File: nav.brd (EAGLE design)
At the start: 160 x 100 mm, 61 parts, among them IC1 FT230XQ, SW1 DHT-4235A, U2 ATMEGA2560-16AU100A-M, U3 MPL3115A2, Y1 16MHz

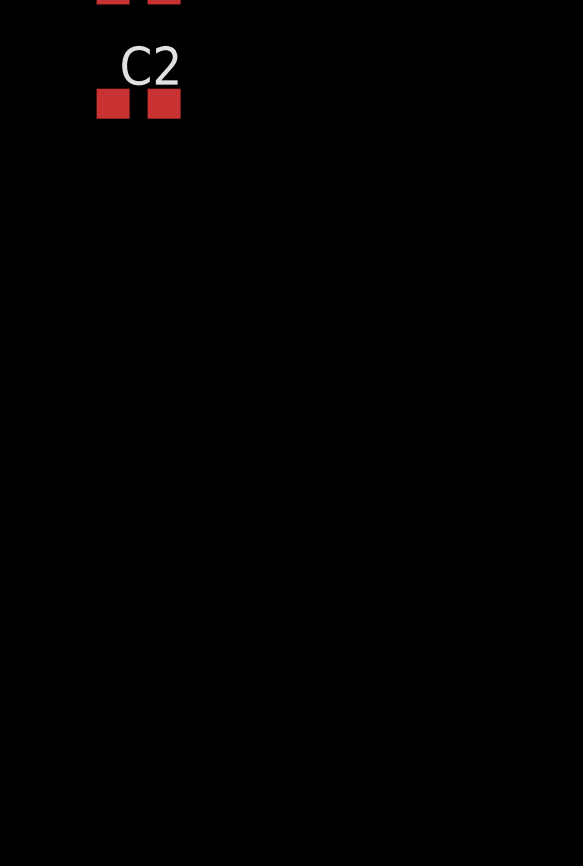
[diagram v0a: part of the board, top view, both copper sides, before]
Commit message: Added Barometer
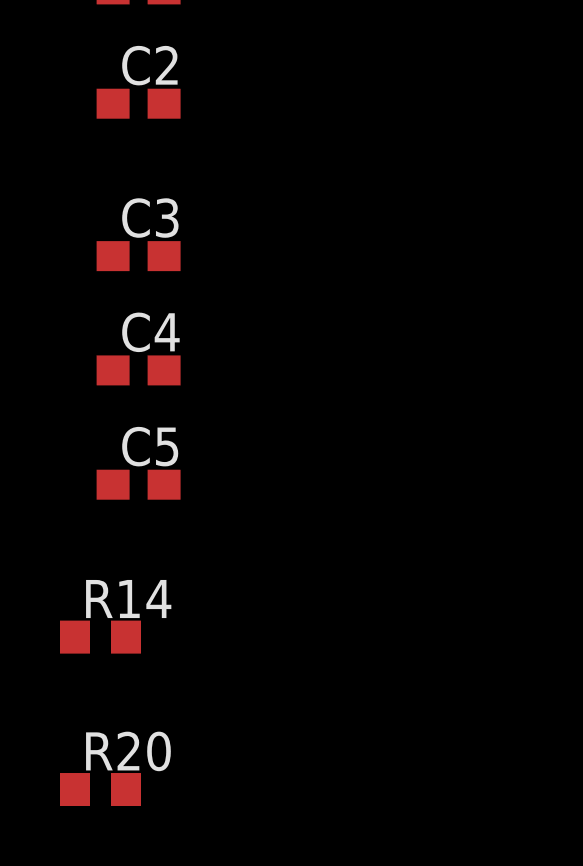
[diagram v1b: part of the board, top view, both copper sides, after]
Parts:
- added C3: 10u, resistor:C0603
- added C4, C5: 100n, resistor:C0603
- added R14, R20: (no value), resistor:R0603
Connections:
- removed net CAP: U3.2
- removed net VDD: U3.1
- removed net VDDIO: U3.4
- new net BARO_INT1: U2.89, U3.6
- new net BARO_INT2: U2.88, U3.5
- new net N$17: C5.1, U3.2
- new net SCL: R14.1, U2.43, U3.8
- new net SDA: R20.1, U2.44, U3.7
- net +3V3: now also C3.1, C4.1, R14.2, R20.2, U3.1, U3.4
- net GND: now also C3.2, C4.2, C5.2
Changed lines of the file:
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@@
 <element name="C1" library="resistor" library_urn="urn:adsk.eagle:library:348" package="C0603" package3d_urn="urn:adsk.eagle:package:23616/2" value="1u" x="-3.81" y="-231.14"/>
 <element name="C2" library="resistor" library_urn="urn:adsk.eagle:library:348" package="C0603" package3d_urn="urn:adsk.eagle:package:23616/2" value="0.01u" x="-3.81" y="-234.95"/>
+<element name="C3" library="resistor" library_urn="urn:adsk.eagle:library:348" package="C0603" package3d_urn="urn:adsk.eagle:package:23616/2" value="10u" x="-3.81" y="-240.03"/>
+<element name="C4" library="resistor" library_urn="urn:adsk.eagle:library:348" package="C0603" package3d_urn="urn:adsk.eagle:package:23616/2" value="100n" x="-3.81" y="-243.84"/>
+<element name="C5" library="resistor" library_urn="urn:adsk.eagle:library:348" package="C0603" package3d_urn="urn:adsk.eagle:package:23616/2" value="100n" x="-3.81" y="-247.65"/>
+<element name="R14" library="resistor" library_urn="urn:adsk.eagle:library:348" package="R0603" package3d_urn="urn:adsk.eagle:package:23555/2" value="" x="-5.08" y="-252.73"/>
+<element name="R20" library="resistor" library_urn="urn:adsk.eagle:library:348" package="R0603" package3d_urn="urn:adsk.eagle:package:23555/2" value="" x="-5.08" y="-257.81"/>
 </elements>
 <signals>
@@
 <contactref element="SW1" pad="4"/>
 <contactref element="SW1" pad="3"/>
-<contactref element="U3" pad="3"/>
 <contactref element="U1" pad="P$3"/>
 <contactref element="U1" pad="P$8"/>
@@
 <contactref element="GPS_ANT" pad="GND@4"/>
 <contactref element="GPS_ANT" pad="GND@3"/>
+<contactref element="U3" pad="3"/>
+<contactref element="C5" pad="2"/>
+<contactref element="C3" pad="2"/>
+<contactref element="C4" pad="2"/>
+<wire x1="-2.96" y1="-243.84" x2="-2.96" y2="-247.65" width="0" layer="19" extent="1-1"/>
+<wire x1="-2.96" y1="-240.03" x2="-2.96" y2="-243.84" width="0" layer="19" extent="1-1"/>
+<wire x1="-2.96" y1="-234.95" x2="-2.96" y2="-240.03" width="0" layer="19" extent="1-1"/>
 <wire x1="-2.96" y1="-231.14" x2="-2.96" y2="-234.95" width="0" layer="19" extent="1-1"/>
 <wire x1="4.572" y1="-212.09" x2="-2.96" y2="-231.14" width="0" layer="19" extent="1-1"/>
@@
 <contactref element="C1" pad="1"/>
 <contactref element="C2" pad="1"/>
+<contactref element="U3" pad="1"/>
+<contactref element="U3" pad="4"/>
+<contactref element="C4" pad="1"/>
+<contactref element="C3" pad="1"/>
+<contactref element="R20" pad="2"/>
+<contactref element="R14" pad="2"/>
+<wire x1="-4.66" y1="-240.03" x2="-4.66" y2="-243.84" width="0" layer="19" extent="1-1"/>
+<wire x1="-4.66" y1="-234.95" x2="-4.66" y2="-240.03" width="0" layer="19" extent="1-1"/>
 <wire x1="-4.66" y1="-231.14" x2="-4.66" y2="-234.95" width="0" layer="19" extent="1-1"/>
 <wire x1="-3.81" y1="-228.08" x2="-4.66" y2="-231.14" width="0" layer="19" extent="1-1"/>
+<wire x1="-4.23" y1="-252.73" x2="-4.66" y2="-243.84" width="0" layer="19" extent="1-1"/>
+<wire x1="-4.23" y1="-257.81" x2="-4.23" y2="-252.73" width="0" layer="19" extent="1-1"/>
 <wire x1="-4.23" y1="-199.39" x2="-3.81" y2="-228.08" width="0" layer="19" extent="1-1"/>
-<wire x1="3.93" y1="-181.21" x2="-4.23" y2="-199.39" width="0" layer="19" extent="1-1"/>
+<wire x1="-5.01" y1="-193.645" x2="-4.23" y2="-199.39" width="0" layer="19" extent="1-1"/>
+<wire x1="-5.01" y1="-189.895" x2="-5.01" y2="-193.645" width="0" layer="19" extent="1-1"/>
+<wire x1="3.93" y1="-181.21" x2="-5.01" y2="-189.895" width="0" layer="19" extent="1-1"/>
 <wire x1="36.41" y1="-168.91" x2="3.93" y2="-181.21" width="0" layer="19" extent="1-1"/>
 <wire x1="2.96" y1="-77.47" x2="36.41" y2="-168.91" width="0" layer="19" extent="1-1"/>
@@
 <wire x1="21.59" y1="-172.2" x2="1.69" y2="-175.26" width="0" layer="19" extent="1-1"/>
 </signal>
-<signal name="VDD">
-<contactref element="U3" pad="1"/>
-</signal>
-<signal name="CAP">
-<contactref element="U3" pad="2"/>
-</signal>
-<signal name="VDDIO">
-<contactref element="U3" pad="4"/>
-</signal>
 <signal name="!GPS_RST">
 <contactref element="U1" pad="P$2"/>
@@
 <wire x1="-4.23" y1="-220.98" x2="-3.81" y2="-226.58" width="0" layer="19" extent="1-1"/>
 </signal>
+<signal name="N$17">
+<contactref element="U3" pad="2"/>
+<contactref element="C5" pad="1"/>
+<wire x1="-5.01" y1="-191.145" x2="-4.66" y2="-247.65" width="0" layer="19" extent="1-1"/>
+</signal>
+<signal name="SCL">
+<contactref element="U3" pad="8"/>
+<contactref element="U2" pad="43"/>
+<contactref element="R14" pad="1"/>
+<wire x1="-5.93" y1="-252.73" x2="-2.61" y2="-189.895" width="0" layer="19" extent="1-1"/>
+<wire x1="13.93" y1="-17.9578" x2="-2.61" y2="-189.895" width="0" layer="19" extent="1-1"/>
+</signal>
+<signal name="SDA">
+<contactref element="U3" pad="7"/>
+<contactref element="U2" pad="44"/>
+<contactref element="R20" pad="1"/>
+<wire x1="-5.93" y1="-257.81" x2="-2.61" y2="-191.145" width="0" layer="19" extent="1-1"/>
+<wire x1="14.43" y1="-17.9578" x2="-2.61" y2="-191.145" width="0" layer="19" extent="1-1"/>
+</signal>
+<signal name="BARO_INT1">
+<contactref element="U3" pad="6"/>
+<contactref element="U2" pad="89"/>
+<wire x1="10.93" y1="-2.3622" x2="-2.61" y2="-192.395" width="0" layer="19" extent="1-1"/>
+</signal>
+<signal name="BARO_INT2">
+<contactref element="U3" pad="5"/>
+<contactref element="U2" pad="88"/>
+<wire x1="11.43" y1="-2.3622" x2="-2.61" y2="-193.645" width="0" layer="19" extent="1-1"/>
+</signal>
 </signals>

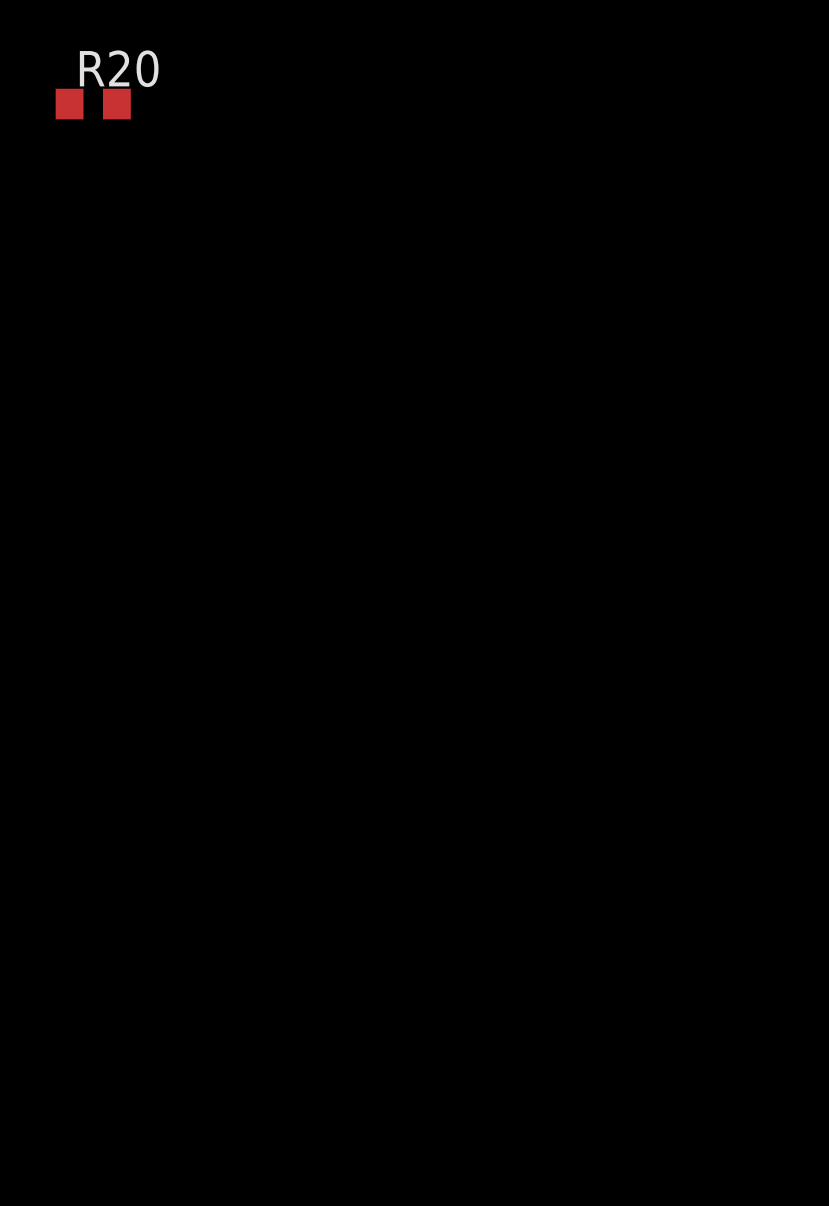
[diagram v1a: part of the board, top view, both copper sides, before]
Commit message: Added LoRa
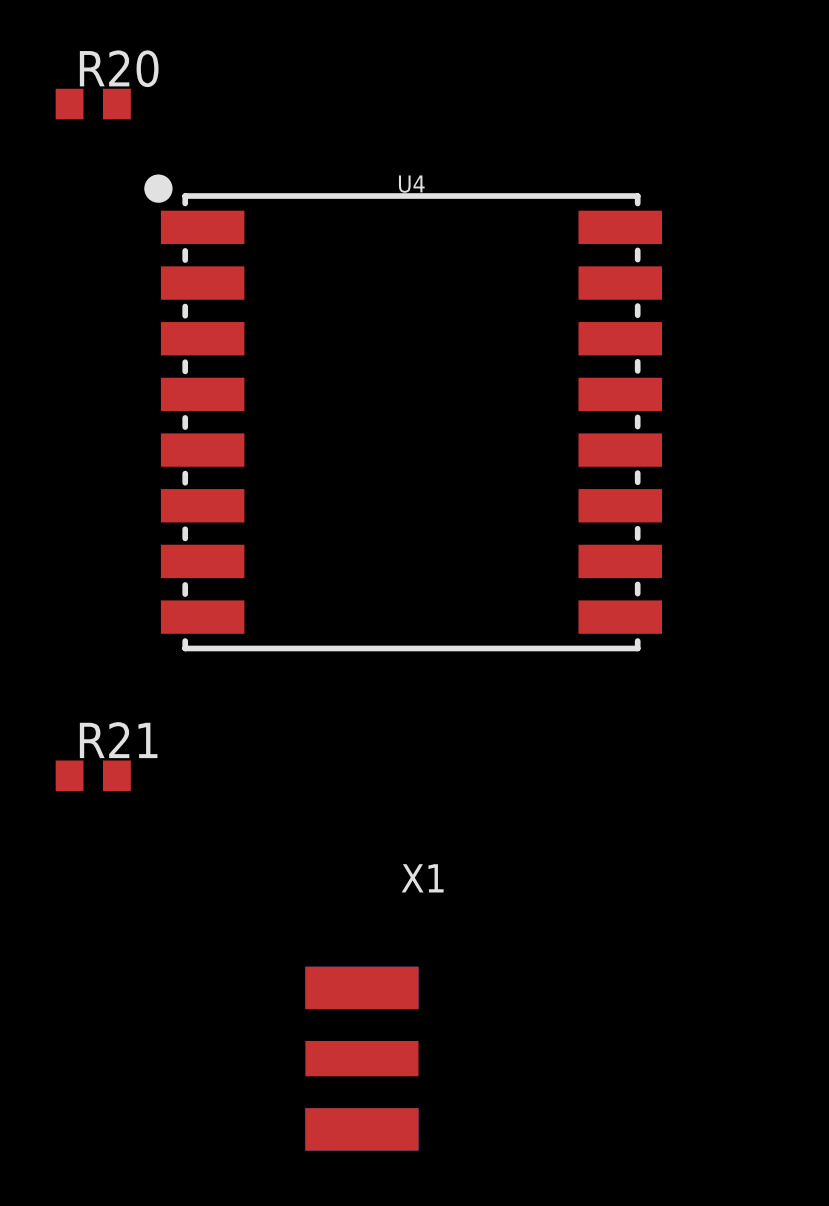
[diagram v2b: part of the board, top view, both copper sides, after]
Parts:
- added R21: (no value), resistor:R0603
- added U4: 433MHz, SparkFun-RF:RFM69HCW-XXXS2
- added X1: (no value), adafruit:SMA_EDGELAUNCH
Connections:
- new net !LORA_RST: R21.1, U2.69, U4.6
- new net !LORA_SS: U2.79, U4.5
- new net LORA_DIO0: U2.63, U4.14
- new net LORA_DIO1: U2.64, U4.15
- new net LORA_DIO2: U2.65, U4.16
- new net LORA_DIO3: U2.66, U4.11
- new net LORA_DIO4: U2.67, U4.12
- new net LORA_DIO5: U2.68, U4.7
- new net N$30: U4.9, X1.P
- net +3V3: now also R21.2, U4.13
- net GND: now also U4.1, U4.10, U4.8, X1.GND@1, X1.GND@2, X1.GND@3, X1.GND@4
- net MISO: now also U4.2
- net MOSI: now also U4.3
- net SCK: now also U4.4
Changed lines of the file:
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@@
 <element name="R14" library="resistor" library_urn="urn:adsk.eagle:library:348" package="R0603" package3d_urn="urn:adsk.eagle:package:23555/2" value="" x="-5.08" y="-252.73"/>
 <element name="R20" library="resistor" library_urn="urn:adsk.eagle:library:348" package="R0603" package3d_urn="urn:adsk.eagle:package:23555/2" value="" x="-5.08" y="-257.81"/>
+<element name="U4" library="SparkFun-RF" library_urn="urn:adsk.eagle:library:531" package="RFM69HCW-XXXS2" package3d_urn="urn:adsk.eagle:package:39566/1" value="433MHz" x="6.35" y="-269.24">
+<attribute name="PROD_ID" value="IC-12053" x="6.35" y="-269.24" size="1.778" layer="27" display="off"/>
+</element>
+<element name="R21" library="resistor" library_urn="urn:adsk.eagle:library:348" package="R0603" package3d_urn="urn:adsk.eagle:package:23555/2" value="" x="-5.08" y="-281.94"/>
+<element name="X1" library="adafruit" library_urn="urn:adsk.eagle:library:420" package="SMA_EDGELAUNCH" value="" x="2.54" y="-292.1"/>
 </elements>
 <signals>
@@
 <contactref element="C3" pad="2"/>
 <contactref element="C4" pad="2"/>
+<contactref element="U4" pad="8"/>
+<contactref element="U4" pad="10"/>
+<contactref element="U4" pad="1"/>
+<contactref element="X1" pad="GND@4"/>
+<contactref element="X1" pad="GND@3"/>
+<contactref element="X1" pad="GND@2"/>
+<contactref element="X1" pad="GND@1"/>
 <wire x1="-2.96" y1="-243.84" x2="-2.96" y2="-247.65" width="0" layer="19" extent="1-1"/>
 <wire x1="-2.96" y1="-240.03" x2="-2.96" y2="-243.84" width="0" layer="19" extent="1-1"/>
 <wire x1="-2.96" y1="-234.95" x2="-2.96" y2="-240.03" width="0" layer="19" extent="1-1"/>
 <wire x1="-2.96" y1="-231.14" x2="-2.96" y2="-234.95" width="0" layer="19" extent="1-1"/>
+<wire x1="-1.15" y1="-262.24" x2="-2.96" y2="-247.65" width="0" layer="19" extent="1-1"/>
+<wire x1="-1.15" y1="-276.24" x2="-1.15" y2="-262.24" width="0" layer="19" extent="1-1"/>
+<wire x1="4.572" y1="-289.56" x2="-1.15" y2="-276.24" width="0" layer="19" extent="1-16"/>
+<wire x1="4.572" y1="-289.56" x2="4.572" y2="-289.56" width="0" layer="19" extent="1-16"/>
+<wire x1="4.572" y1="-294.64" x2="4.572" y2="-289.56" width="0" layer="19" extent="16-16"/>
+<wire x1="4.572" y1="-294.64" x2="4.572" y2="-294.64" width="0" layer="19" extent="1-16"/>
+<wire x1="13.85" y1="-274.24" x2="-1.15" y2="-276.24" width="0" layer="19" extent="1-1"/>
 <wire x1="4.572" y1="-212.09" x2="-2.96" y2="-231.14" width="0" layer="19" extent="1-1"/>
 <wire x1="4.572" y1="-212.09" x2="4.572" y2="-212.09" width="0" layer="19" extent="1-16"/>
@@
 <contactref element="ISP" pad="1"/>
 <contactref element="U2" pad="22"/>
+<contactref element="U4" pad="2"/>
 <wire x1="3.6322" y1="-14.66" x2="7.62" y2="-30.48" width="0" layer="19" extent="1-1"/>
+<wire x1="-1.15" y1="-264.24" x2="7.62" y2="-30.48" width="0" layer="19" extent="1-1"/>
 </signal>
 <signal name="SCK">
 <contactref element="ISP" pad="3"/>
 <contactref element="U2" pad="20"/>
+<contactref element="U4" pad="4"/>
 <wire x1="3.6322" y1="-13.66" x2="10.16" y2="-30.48" width="0" layer="19" extent="1-1"/>
+<wire x1="-1.15" y1="-268.24" x2="10.16" y2="-30.48" width="0" layer="19" extent="1-1"/>
 </signal>
 <signal name="MOSI">
 <contactref element="ISP" pad="4"/>
 <contactref element="U2" pad="21"/>
+<contactref element="U4" pad="3"/>
 <wire x1="3.6322" y1="-14.16" x2="10.16" y2="-27.94" width="0" layer="19" extent="1-1"/>
+<wire x1="-1.15" y1="-266.24" x2="10.16" y2="-27.94" width="0" layer="19" extent="1-1"/>
 </signal>
 <signal name="N$2">
@@
 <contactref element="R20" pad="2"/>
 <contactref element="R14" pad="2"/>
+<contactref element="U4" pad="13"/>
+<contactref element="R21" pad="2"/>
 <wire x1="-4.66" y1="-240.03" x2="-4.66" y2="-243.84" width="0" layer="19" extent="1-1"/>
 <wire x1="-4.66" y1="-234.95" x2="-4.66" y2="-240.03" width="0" layer="19" extent="1-1"/>
@@
 <wire x1="-4.23" y1="-252.73" x2="-4.66" y2="-243.84" width="0" layer="19" extent="1-1"/>
 <wire x1="-4.23" y1="-257.81" x2="-4.23" y2="-252.73" width="0" layer="19" extent="1-1"/>
+<wire x1="13.85" y1="-268.24" x2="-4.23" y2="-257.81" width="0" layer="19" extent="1-1"/>
+<wire x1="-4.23" y1="-281.94" x2="13.85" y2="-268.24" width="0" layer="19" extent="1-1"/>
 <wire x1="-4.23" y1="-199.39" x2="-3.81" y2="-228.08" width="0" layer="19" extent="1-1"/>
 <wire x1="-5.01" y1="-193.645" x2="-4.23" y2="-199.39" width="0" layer="19" extent="1-1"/>
@@
 <wire x1="11.43" y1="-2.3622" x2="-2.61" y2="-193.645" width="0" layer="19" extent="1-1"/>
 </signal>
+<signal name="!LORA_SS">
+<contactref element="U4" pad="5"/>
+<contactref element="U2" pad="79"/>
+<wire x1="15.93" y1="-2.3622" x2="-1.15" y2="-270.24" width="0" layer="19" extent="1-1"/>
+</signal>
+<signal name="N$30">
+<contactref element="U4" pad="9"/>
+<contactref element="X1" pad="P"/>
+<wire x1="13.85" y1="-276.24" x2="4.572" y2="-292.1" width="0" layer="19" extent="1-1"/>
+</signal>
+<signal name="LORA_DIO5">
+<contactref element="U4" pad="7"/>
+<contactref element="U2" pad="68"/>
+<wire x1="19.2278" y1="-7.66" x2="-1.15" y2="-274.24" width="0" layer="19" extent="1-1"/>
+</signal>
+<signal name="LORA_DIO4">
+<contactref element="U4" pad="12"/>
+<contactref element="U2" pad="67"/>
+<wire x1="13.85" y1="-270.24" x2="19.2278" y2="-8.16" width="0" layer="19" extent="1-1"/>
+</signal>
+<signal name="LORA_DIO3">
+<contactref element="U4" pad="11"/>
+<contactref element="U2" pad="66"/>
+<wire x1="13.85" y1="-272.24" x2="19.2278" y2="-8.66" width="0" layer="19" extent="1-1"/>
+</signal>
+<signal name="LORA_DIO2">
+<contactref element="U4" pad="16"/>
+<contactref element="U2" pad="65"/>
+<wire x1="19.2278" y1="-9.16" x2="13.85" y2="-262.24" width="0" layer="19" extent="1-1"/>
+</signal>
+<signal name="LORA_DIO1">
+<contactref element="U4" pad="15"/>
+<contactref element="U2" pad="64"/>
+<wire x1="19.2278" y1="-9.66" x2="13.85" y2="-264.24" width="0" layer="19" extent="1-1"/>
+</signal>
+<signal name="LORA_DIO0">
+<contactref element="U4" pad="14"/>
+<contactref element="U2" pad="63"/>
+<wire x1="19.2278" y1="-10.16" x2="13.85" y2="-266.24" width="0" layer="19" extent="1-1"/>
+</signal>
+<signal name="!LORA_RST">
+<contactref element="U2" pad="69"/>
+<contactref element="U4" pad="6"/>
+<contactref element="R21" pad="1"/>
+<wire x1="-1.15" y1="-272.24" x2="-5.93" y2="-281.94" width="0" layer="19" extent="1-1"/>
+<wire x1="19.2278" y1="-7.16" x2="-1.15" y2="-272.24" width="0" layer="19" extent="1-1"/>
+</signal>
 </signals>
